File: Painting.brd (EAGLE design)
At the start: 53 x 81.3 mm, 12 parts, among them U1 ATTINY85-20P

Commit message: First Draft
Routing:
- net +UB: track 0.00 -> 119.1 mm
- net -UB: track 0.00 -> 102.7 mm
- net RCLK: track 119.1 -> 124.2 mm

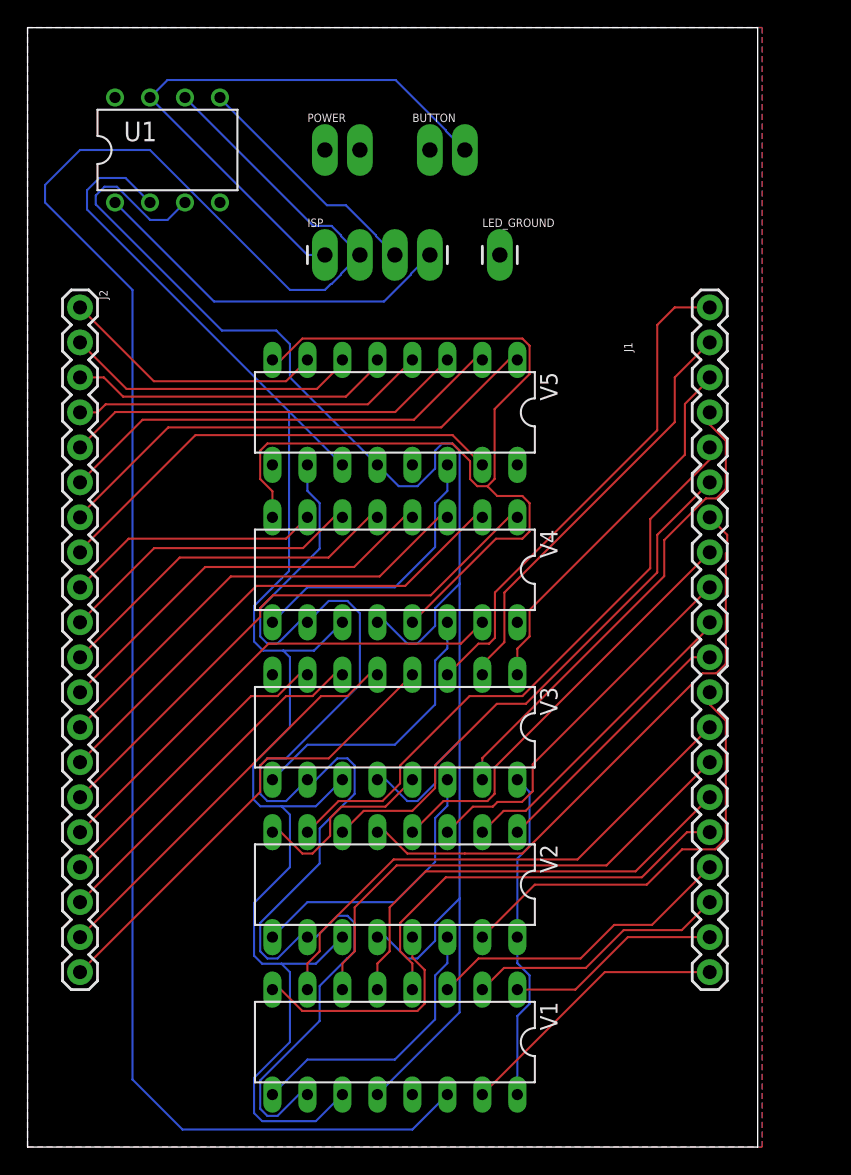
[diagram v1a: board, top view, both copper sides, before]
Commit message: Removing 90 degrees in traces
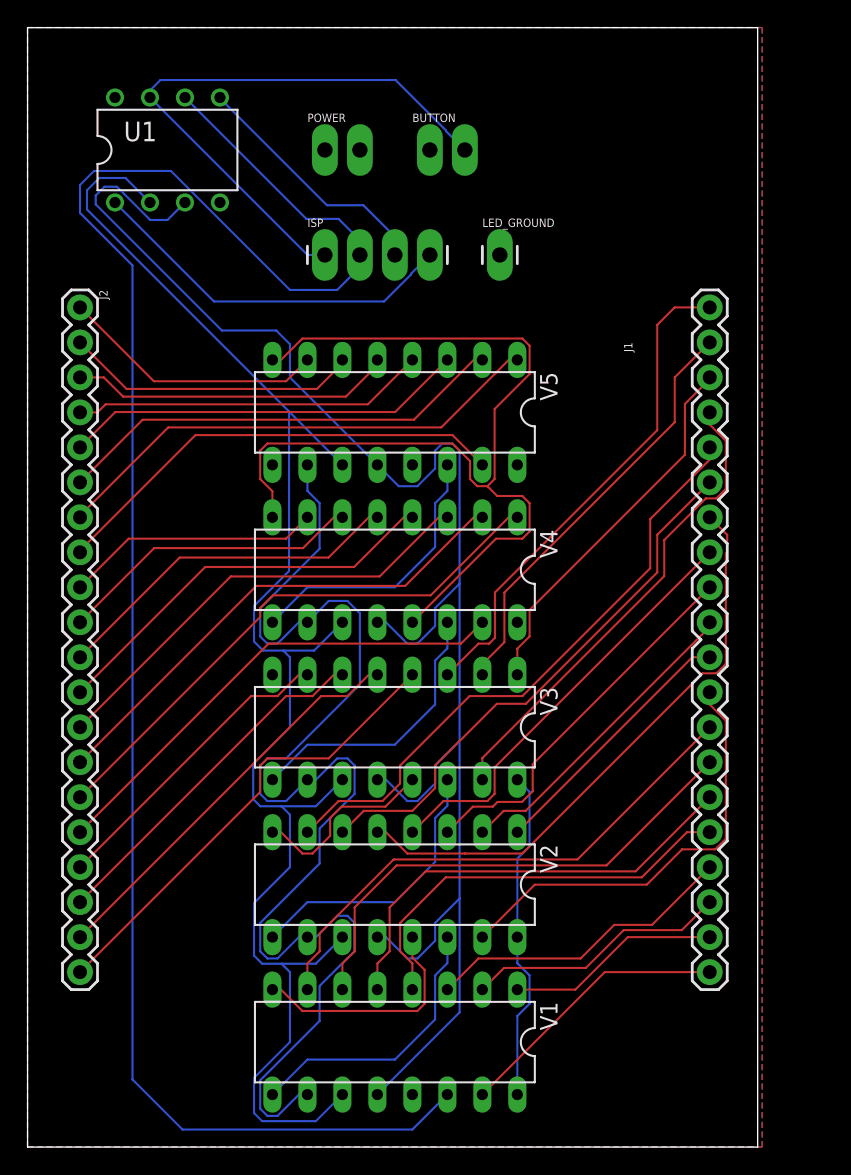
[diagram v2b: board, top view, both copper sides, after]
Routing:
- net DATA/MISO: track 139.7 -> 135.9 mm
- net MOSI: track 17.5 -> 18.2 mm
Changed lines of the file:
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@@
 <wire x1="21.59" y1="63.5" x2="20.32" y2="63.5" width="0.1524" layer="16"/>
 <wire x1="20.32" y1="63.5" x2="8.89" y2="74.93" width="0.1524" layer="16"/>
-<wire x1="8.89" y1="74.93" x2="10.16" y2="76.2" width="0.1524" layer="16"/>
+<wire x1="8.89" y1="74.93" x2="8.89" y2="75.438" width="0.1524" layer="16"/>
+<wire x1="9.652" y1="76.2" x2="8.89" y2="75.438" width="0.1524" layer="16"/>
 <wire x1="30.3784" y1="72.54376875" x2="30.3784" y2="72.4916" width="0.1524" layer="16"/>
 <wire x1="30.3784" y1="72.4916" x2="31.75" y2="71.12" width="0.1524" layer="16"/>
 <wire x1="26.72216875" y1="76.2" x2="30.3784" y2="72.54376875" width="0.1524" layer="16"/>
-<wire x1="10.16" y1="76.2" x2="26.72216875" y2="76.2" width="0.1524" layer="16"/>
+<wire x1="9.652" y1="76.2" x2="26.72216875" y2="76.2" width="0.1524" layer="16"/>
 </signal>
 <signal name="MOSI">
 <contactref element="ISP" pad="3"/>
 <contactref element="U1" pad="5"/>
-<wire x1="26.67" y1="63.5" x2="25.2984" y2="64.8716" width="0.1524" layer="16"/>
-<wire x1="25.2984" y1="64.8716" x2="25.2984" y2="64.92376875" width="0.1524" layer="16"/>
+<wire x1="26.67" y1="63.5" x2="26.67" y2="64.82216875" width="0.1524" layer="16"/>
+<wire x1="26.67" y1="64.82216875" x2="24.38536875" y2="67.1068" width="0.1524" layer="16"/>
 <wire x1="21.74103125" y1="67.1068" x2="13.97" y2="74.87783125" width="0.1524" layer="16"/>
 <wire x1="13.97" y1="74.93" x2="13.97" y2="74.87783125" width="0.1524" layer="16"/>
-<wire x1="25.2984" y1="64.92376875" x2="23.11536875" y2="67.1068" width="0.1524" layer="16"/>
-<wire x1="23.11536875" y1="67.1068" x2="21.74103125" y2="67.1068" width="0.1524" layer="16"/>
+<wire x1="24.38536875" y1="67.1068" x2="21.74103125" y2="67.1068" width="0.1524" layer="16"/>
 </signal>
 <signal name="DATA/MISO">
@@
 <contactref element="V1" pad="14"/>
 <contactref element="ISP" pad="2"/>
-<wire x1="24.13" y1="63.5" x2="22.7584" y2="64.8716" width="0.1524" layer="16"/>
-<wire x1="22.7584" y1="64.8716" x2="22.7584" y2="64.92376875" width="0.1524" layer="16"/>
-<wire x1="22.7584" y1="64.92376875" x2="22.07396875" y2="65.6082" width="0.1524" layer="16"/>
-<wire x1="22.07396875" y1="65.6082" x2="20.7518" y2="65.6082" width="0.1524" layer="16"/>
-<wire x1="20.7518" y1="65.6082" x2="11.43" y2="74.93" width="0.1524" layer="16"/>
-<wire x1="24.13" y1="63.5" x2="22.7584" y2="62.1284" width="0.1524" layer="16"/>
-<wire x1="22.7584" y1="62.1284" x2="22.7584" y2="62.07623125" width="0.1524" layer="16"/>
-<wire x1="22.7584" y1="62.07623125" x2="22.07396875" y2="61.3918" width="0.1524" layer="16"/>
-<wire x1="22.07396875" y1="61.3918" x2="22.0218" y2="61.3918" width="0.1524" layer="16"/>
-<wire x1="22.0218" y1="61.3918" x2="21.59" y2="60.96" width="0.1524" layer="16"/>
-<wire x1="21.59" y1="60.96" x2="19.05" y2="60.96" width="0.1524" layer="16"/>
-<wire x1="19.05" y1="60.96" x2="8.89" y2="71.12" width="0.1524" layer="16"/>
-<wire x1="8.89" y1="71.12" x2="3.81" y2="71.12" width="0.1524" layer="16"/>
-<wire x1="3.81" y1="71.12" x2="1.27" y2="68.58" width="0.1524" layer="16"/>
-<wire x1="1.27" y1="68.58" x2="1.27" y2="67.31" width="0.1524" layer="16"/>
-<wire x1="1.27" y1="67.31" x2="7.62" y2="60.96" width="0.1524" layer="16"/>
+<wire x1="24.13" y1="63.5" x2="24.13" y2="64.56816875" width="0.1524" layer="16"/>
+<wire x1="24.13" y1="64.56816875" x2="22.58196875" y2="66.1162" width="0.1524" layer="16"/>
+<wire x1="22.58196875" y1="66.1162" x2="20.2438" y2="66.1162" width="0.1524" layer="16"/>
+<wire x1="20.2438" y1="66.1162" x2="11.43" y2="74.93" width="0.1524" layer="16"/>
+<wire x1="24.13" y1="63.5" x2="24.13" y2="62.611" width="0.1524" layer="16"/>
+<wire x1="24.13" y1="62.611" x2="22.479" y2="60.96" width="0.1524" layer="16"/>
+<wire x1="22.479" y1="60.96" x2="19.05" y2="60.96" width="0.1524" layer="16"/>
+<wire x1="19.05" y1="60.96" x2="10.414" y2="69.596" width="0.1524" layer="16"/>
+<wire x1="10.414" y1="69.596" x2="4.826" y2="69.596" width="0.1524" layer="16"/>
+<wire x1="4.826" y1="69.596" x2="3.81" y2="68.58" width="0.1524" layer="16"/>
+<wire x1="3.81" y1="68.58" x2="3.81" y2="66.548" width="0.1524" layer="16"/>
+<wire x1="3.81" y1="66.548" x2="7.62" y2="62.738" width="0.1524" layer="16"/>
 <wire x1="7.62" y1="3.6322" x2="11.2522" y2="0" width="0.1524" layer="16"/>
-<wire x1="7.62" y1="60.96" x2="7.62" y2="3.6322" width="0.1524" layer="16"/>
+<wire x1="7.62" y1="62.738" x2="7.62" y2="3.6322" width="0.1524" layer="16"/>
 <wire x1="11.2522" y1="0" x2="27.94" y2="0" width="0.1524" layer="16"/>
 <wire x1="27.94" y1="0" x2="30.48" y2="2.54" width="0.1524" layer="16"/>

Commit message: Increased trace spacing and deleted backup files
Read the commit message title
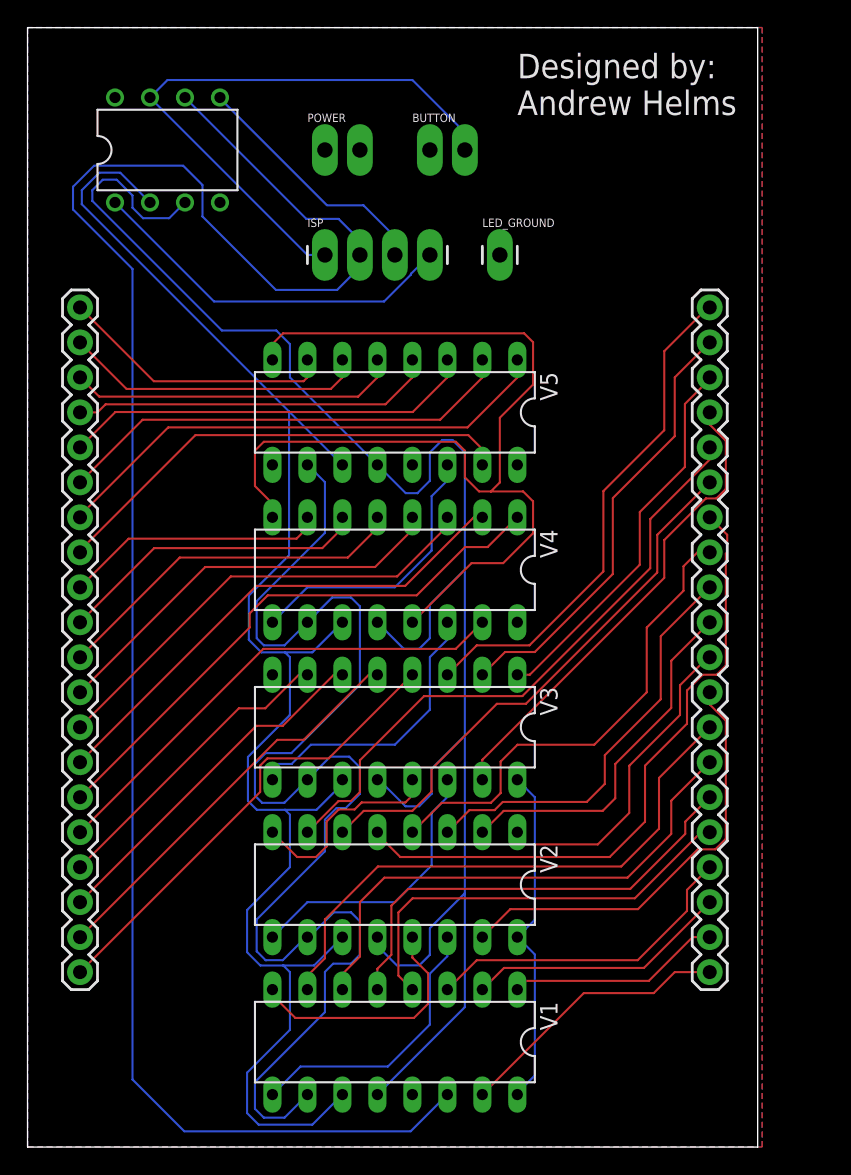
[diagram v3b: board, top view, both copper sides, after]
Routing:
- net RCLK: track 124.2 -> 131.8 mm
- net +UB: track 119.1 -> 125.7 mm
- net -UB: track 102.7 -> 108.4 mm
- net 9: track 19.2 -> 23.6 mm
- net 13: track 42.9 -> 47.0 mm
- net 12: track 31.1 -> 35.1 mm
- net SRCLK: track 117.4 -> 120.7 mm
- net 10: track 23.0 -> 26.3 mm
- net 11: track 27.6 -> 30.3 mm
- net 7: track 39.0 -> 41.5 mm
- net DATA/MISO: track 135.9 -> 138.3 mm
- net 6: track 36.5 -> 37.9 mm
- net 18: track 31.0 -> 32.2 mm
- net 3: track 22.7 -> 23.6 mm
- net 34: track 32.9 -> 33.6 mm
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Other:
- board text added: "Designed by: Andrew Helms"

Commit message: Connected another trace and wrote some more words
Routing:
- net -UB: track 108.4 -> 109.8 mm
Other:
- board text added: "Designed by: Andrew Helms In collab with: Sarah Bass"
- board text added: "JLCJLCJLCJLC"
- board text removed: "Designed by: Andrew Helms"
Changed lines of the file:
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@@
 <drawing>
 <settings>
-<setting alwaysvectorfont="no"/>
+<setting alwaysvectorfont="yes"/>
 <setting verticaltext="up"/>
 </settings>
@@
 <wire x1="53.01" y1="80" x2="0" y2="80" width="0" layer="20"/>
 <wire x1="0" y1="80" x2="0" y2="-1.27" width="0" layer="20"/>
-<text x="35.56" y="73.66" size="1.778" layer="21">Designed by:
-Andrew Helms</text>
+<text x="34.29" y="68.58" size="1.778" layer="21">Designed by:
+Andrew Helms
+In collab with:
+Sarah Bass</text>
+<text x="50.8" y="76.2" size="1.778" layer="22" rot="MR0">JLCJLCJLCJLC</text>
 </plain>
 <attributes>
@@
 <wire x1="18.5547625" y1="57.8104" x2="17.78" y2="57.0356375" width="0.1524" layer="1"/>
 <wire x1="17.78" y1="55.88" x2="17.78" y2="57.0356375" width="0.1524" layer="1"/>
-<wire x1="17.1577625" y1="49.9364" x2="31.1022375" y2="49.9364" width="0.1524" layer="1"/>
+<wire x1="17.1577625" y1="49.9364" x2="26.67" y2="49.9364" width="0.1524" layer="1"/>
+<wire x1="29.21" y1="49.9364" x2="31.1022375" y2="49.9364" width="0.1524" layer="1"/>
 <wire x1="34.29" y1="46.9773625" x2="34.29" y2="51.6763625" width="0.1524" layer="1"/>
 <wire x1="34.29" y1="51.6763625" x2="36.703" y2="54.0893625" width="0.1524" layer="1"/>
@@
 <wire x1="21.717" y1="22.3646375" x2="22.5933625" y2="23.241" width="0.1524" layer="1"/>
 <wire x1="22.5933625" y1="23.241" x2="23.749" y2="23.241" width="0.1524" layer="1"/>
-<wire x1="17.78" y1="44.45" x2="27.94" y2="48.26" width="0" layer="19" extent="1-1"/>
+<wire x1="27.94" y1="48.6664" x2="29.21" y2="49.9364" width="0.1524" layer="1"/>
+<wire x1="27.94" y1="48.26" x2="27.94" y2="48.6664" width="0.1524" layer="1"/>
+<wire x1="27.94" y1="48.6664" x2="26.67" y2="49.9364" width="0.1524" layer="1"/>
 </signal>
 <signal name="39">
